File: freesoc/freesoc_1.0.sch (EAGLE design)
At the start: 72 parts, among them IC1 CY8C3X66AXI, IC2 CY7C68015A, IC3 REG1117, IC4 24LC00OT, P1 M20-7820842, P5 M20-7820842, Y2 ATS240C, Y3 ST2012SB32768H5HPWAA, Y4 ATS240C

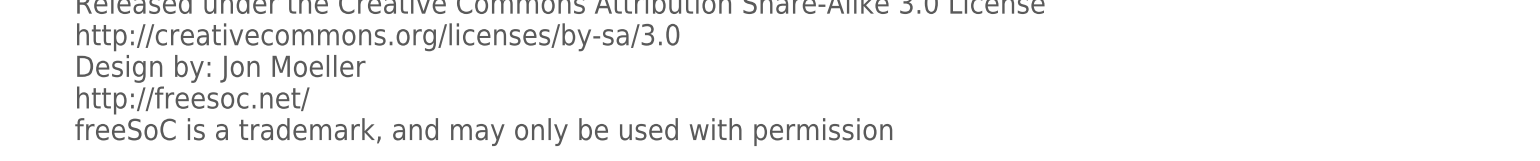
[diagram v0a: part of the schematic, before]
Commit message: DFM changes to freeSoC
Updated board for 7/7mil trace/space.

All vias are now tented.

Updated FX2 QFN pad land for improved reliability
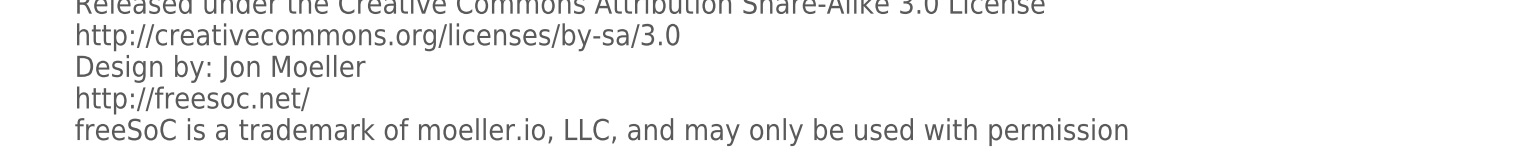
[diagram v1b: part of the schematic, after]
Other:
- note added: "freeSoC is a trademark of moeller.io, LLC, and may only be used with permission"
- note removed: "freeSoC is a trademark, and may only be used with permission"
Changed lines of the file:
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@@
 <?xml version="1.0" encoding="utf-8"?>
 <!DOCTYPE eagle SYSTEM "eagle.dtd">
-<eagle version="6.1">
+<eagle version="6.2">
 <drawing>
 <settings>
@@
 <text x="27.94" y="-172.72" size="5.08" layer="97" font="vector">Design by: Jon Moeller</text>
 <text x="27.94" y="-180.34" size="5.08" layer="97" font="vector">http://freesoc.net/</text>
-<text x="27.94" y="-187.96" size="5.08" layer="97" font="vector">freeSoC is a trademark, and may only be used with permission</text>
+<text x="27.94" y="-187.96" size="5.08" layer="97" font="vector">freeSoC is a trademark of moeller.io, LLC, and may only be used with permission</text>
 <text x="27.94" y="-147.32" size="6.4516" layer="97" font="vector">freeSoC Development Kit v1.0</text>
 <text x="66.294" y="-140.462" size="2.1844" layer="97" font="vector">TM</text>

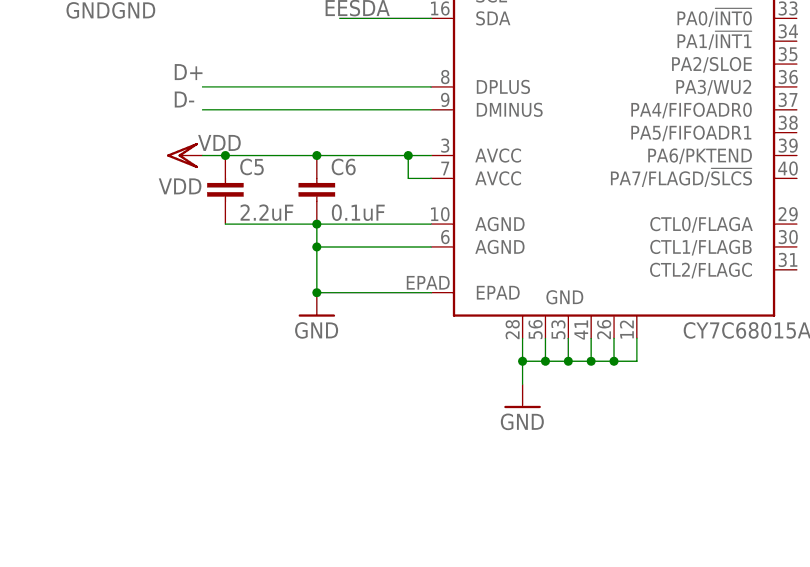
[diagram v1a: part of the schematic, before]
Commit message: More DFM changes
Updated FX2 QFN package thermal pad dimensions to meet Cypress spec.

Added tented vias on thermal pad, appropriate solder paste mask, and
opened vias on bottom to eliminate outgassing
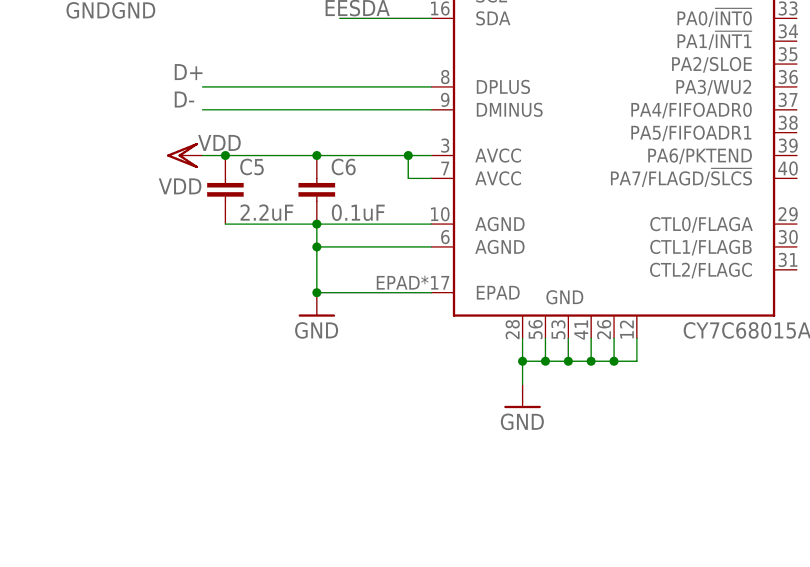
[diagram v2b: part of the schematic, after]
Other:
- moved on the sheet: IC2

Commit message: Updates to boards for production
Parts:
- removed C13: 10nF, SparkFun:CAP0402-CAP
- removed IC3: REG1117, burr-brown:REG1117
- removed P1, P5: M20-7820842, pinhead:PINHD-1X8
- removed R4: 100k, SparkFun:RESISTOR0402-RES
- added C23: 10uF, SparkFun:CAP1206
- added D1, D3: STPS1L30A, SparkFun:DIODE-SCHOTTKY_
- added JP10, JP7, JP8, JP9: M20-7820842, SparkFun:M081X08
- added JP6: 455-1749-1-ND, SparkFun:M02-JST-2MM-SMT
- added U$1: LP2989, SparkFun:LP2989
- C2: value 10uF -> 10nF C0G; device SparkFun:CAP_POL1206 -> SparkFun:CAP0402-CAP
- C3: value 100uF -> 10uF; device SparkFun:CAP_POL6032 -> SparkFun:CAP1206
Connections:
- removed net N$10: C4.2, R3.2, U$5.MTN1, U$5.MTN2, U$5.MTN3
- removed net N$16: C13.2, R4.2, U$6.MTN1, U$6.MTN2, U$6.MTN3, U$6.MTN4
- new net N$13: C2.1, U$1.BYPASS
- new net N$2: D1.A, JP6.2
- new net SHIELD: C4.2, R3.2, U$5.MTN1, U$5.MTN2, U$5.MTN3, U$6.MTN1, U$6.MTN2, U$6.MTN3, U$6.MTN4
- net GND: now also C2.2, C23.2, C3.2, D3.A, JP6.1, JP7.2, JP9.2, U$1.GND; no longer C13.1, C2.-, C3.-, IC3.GND, P5.7, R4.1
- net P12: now also JP7.4, JP9.4; no longer P5.5
- net P120: now also JP10.8, JP8.8; no longer P1.1
- net P121: now also JP10.7, JP8.7; no longer P1.2
- net P122: now also JP10.6, JP8.6; no longer P1.3
- net P123: now also JP10.5, JP8.5; no longer P1.4
- net P124: now also JP10.4, JP8.4; no longer P1.5
- net P125: now also JP10.3, JP8.3; no longer P1.6
- net P126: now also JP10.2, JP8.2; no longer P1.7
- net P127: now also JP10.1, JP8.1; no longer P1.8
- net P14: now also JP7.3, JP9.3; no longer P5.6
- net P15: now also JP7.1, JP9.1; no longer P5.8
- net P50: now also JP7.8, JP9.8; no longer P5.1
- net P51: now also JP7.7, JP9.7; no longer P5.2
- net P52: now also JP7.6, JP9.6; no longer P5.3
- net P53: now also JP7.5, JP9.5; no longer P5.4
- net VDD: now also C23.1, U$1.SENSE, U$1.VOUT; no longer C3.+, IC3.VOUT
- net VIN: now also C3.1, D1.C, D3.C, U$1.!SHUTDOWN, U$1.VIN; no longer C2.+, IC3.VIN
